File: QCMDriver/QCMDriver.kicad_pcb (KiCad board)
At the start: 2 copper layers, 43 x 33 mm, 26 parts, among them J1 Conn_Coaxial, J2 Conn_Coaxial, J3 Conn_Coaxial, Q1 BC817, U1 74LVC1GU04DRL, U2 74LVC1GU04DRL

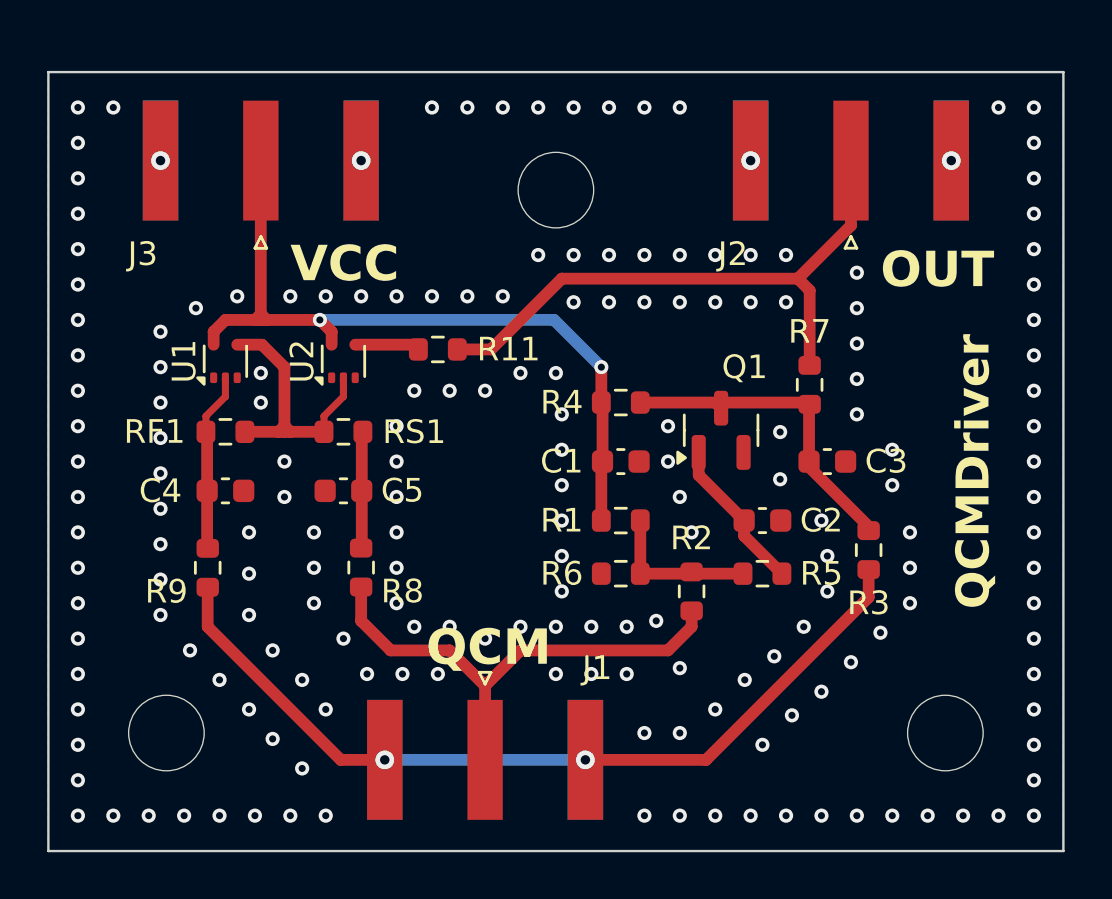
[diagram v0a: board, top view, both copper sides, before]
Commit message: vcc caps and vias added, minor layout improvements
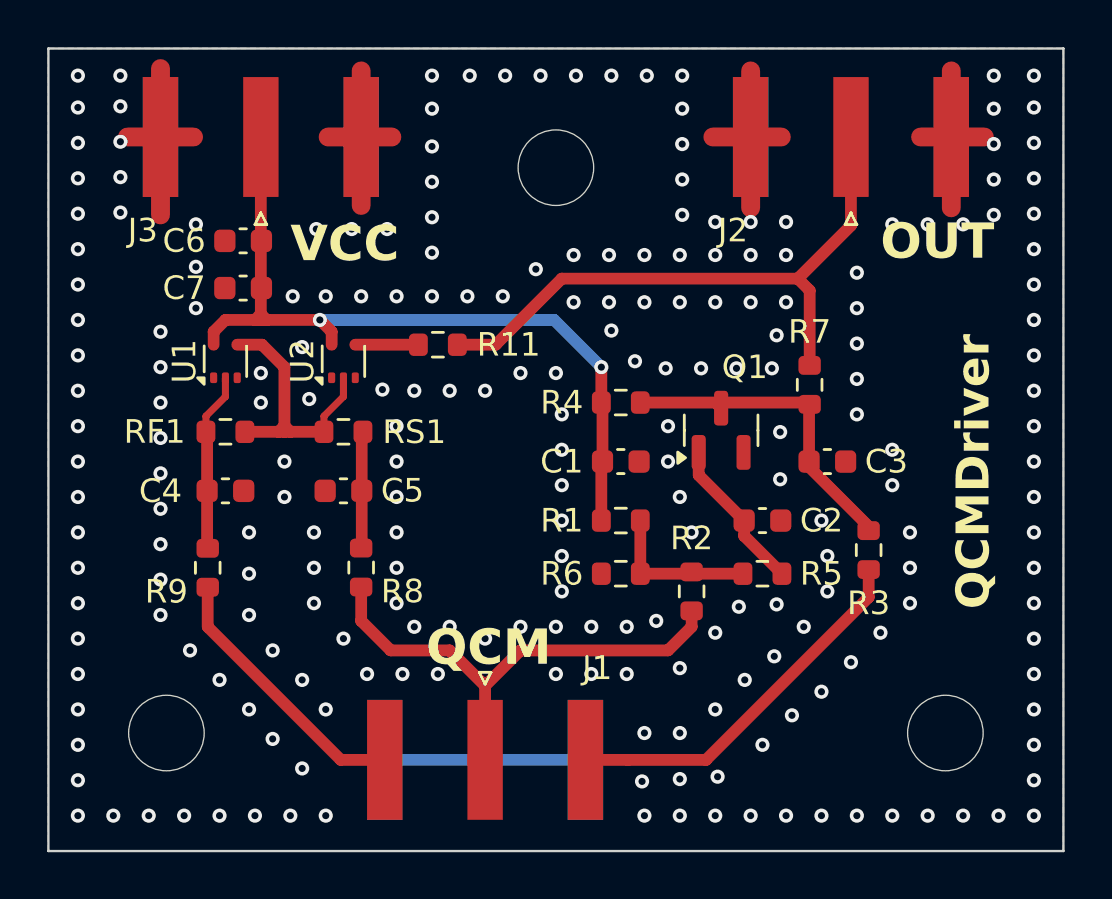
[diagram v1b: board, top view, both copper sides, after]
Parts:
- added C6: 10uF, Capacitor_SMD:C_0603_1608Metric, F.Cu at (112.5, 92.4)
- added C7: 100nF, Capacitor_SMD:C_0603_1608Metric, F.Cu at (112.5, 94.4)
- C1: value 100n -> 100nF
- C2: value 100p -> 100pF
- C3: value 27p -> 27pF
- C4, C5: value 32p -> 32pF
- moved J2 1.00 mm to (138.2, 88.0)
- moved J3 1.00 mm to (113.2, 88.0)
- moved H2 0.95 mm to (125.8, 89.3)
- moved R11 0.20 mm to (120.8, 96.8)
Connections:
- net /VCCOSC renamed VCCOSC
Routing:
- net GND: track 0.00 -> 34.8 mm, vias 188 -> 229
- net /QCMB: vias 2 -> 0
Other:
- board size 43 x 33 mm -> 43 x 34 mm

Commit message: misc improvements
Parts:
- moved R2 3.21 mm to (128.5, 108.4), turned to 0 degrees
- moved R3 2.78 mm to (136.4, 104.5)
- moved R5 2.72 mm to (131.8, 106.8), turned to 90 degrees
- moved C2 1.95 mm to (132.6, 103.8)
- moved J2 1.25 mm to (137.0, 88.0)
- moved H1 1.05 mm to (141.2, 113.3)
- moved R9 0.72 mm to (111.0, 105.5)
- moved R8 0.71 mm to (117.5, 105.5)
- moved R11 0.65 mm to (120.1, 96.8)
- moved H2 0.50 mm to (125.2, 89.3)
- moved C4 0.49 mm to (111.8, 102.5)
- moved C5 0.49 mm to (116.8, 102.5)
- moved R1 0.45 mm to (128.5, 103.8)
- moved R6 0.40 mm to (128.5, 106.1)
- moved C3 0.35 mm to (137.2, 101.4)
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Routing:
- net /QCMA: track 21.4 -> 17.8 mm
- net Net-(Q1-C): track 14.1 -> 11.8 mm
- net Net-(Q1-B): track 6.60 -> 4.68 mm
- net /OUT_OSC: track 25.0 -> 26.6 mm
- net VCCOSC: track 33.0 -> 32.3 mm
- net Net-(R11-Pad1): track 2.76 -> 2.03 mm
- net Net-(C4-Pad1): track 7.60 -> 6.87 mm
- net Net-(R1-Pad2): track 6.66 -> 7.39 mm
- net Net-(C5-Pad1): track 4.96 -> 4.24 mm
- net /QCMB: track 36.0 -> 36.7 mm
- net GND: track 34.8 -> 35.0 mm, vias 229 -> 218
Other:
- board size 43 x 34 mm -> 42 x 34 mm
- board text added: "JLCJLCJLCJLC"
